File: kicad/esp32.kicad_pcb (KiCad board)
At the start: 2 copper layers, 85 x 75 mm, 75 parts, among them J1 5 / 12V, J10 Red, J11 Green, J12 Blue, J13 White, J14 Pad, J15 CONN FT232RL, J16 RJ12-I2C, J17 RJ12-I2C, J18 BATT, J2 +12V, J3 Onewire, J4 Onewire, J5 hole, J6 hole, J7 hole, J8 hole, J9 IO_RGBW, Q1 BSP75, Q2 BSP75, Q3 BSP75, Q4 BSP75, SW1 RESET, SW2 PROG, U1 ESP32-WROOM-32U, U2 MS5637, U3 Si7020-A20, U4 MCP73831-2, U5 ACT4088, U6 ACT4088

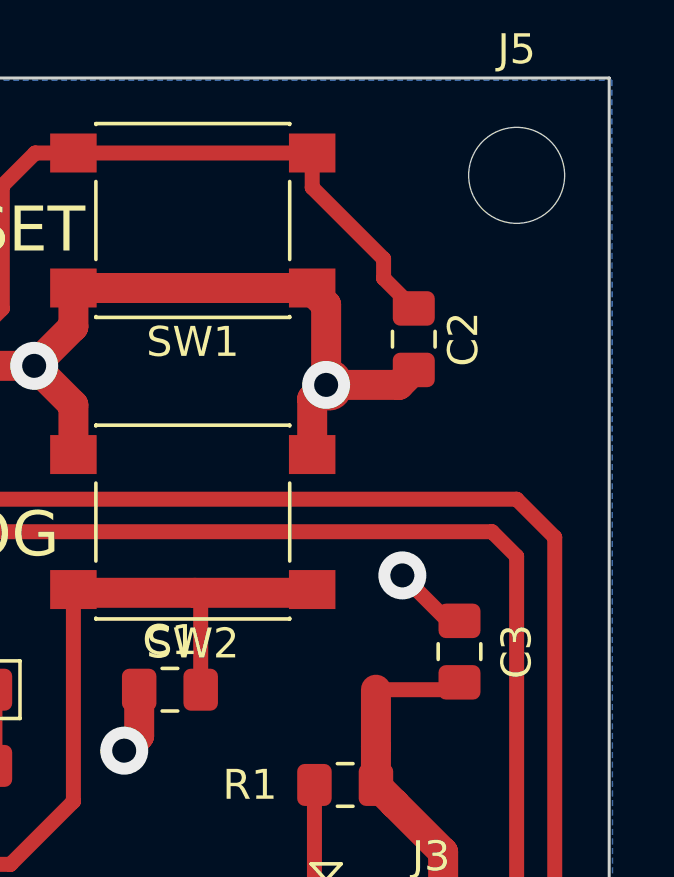
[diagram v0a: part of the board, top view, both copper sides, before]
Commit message: fix: pullup on reset close: https://github.com/Hackuarium/esp-32wroom/issues/1
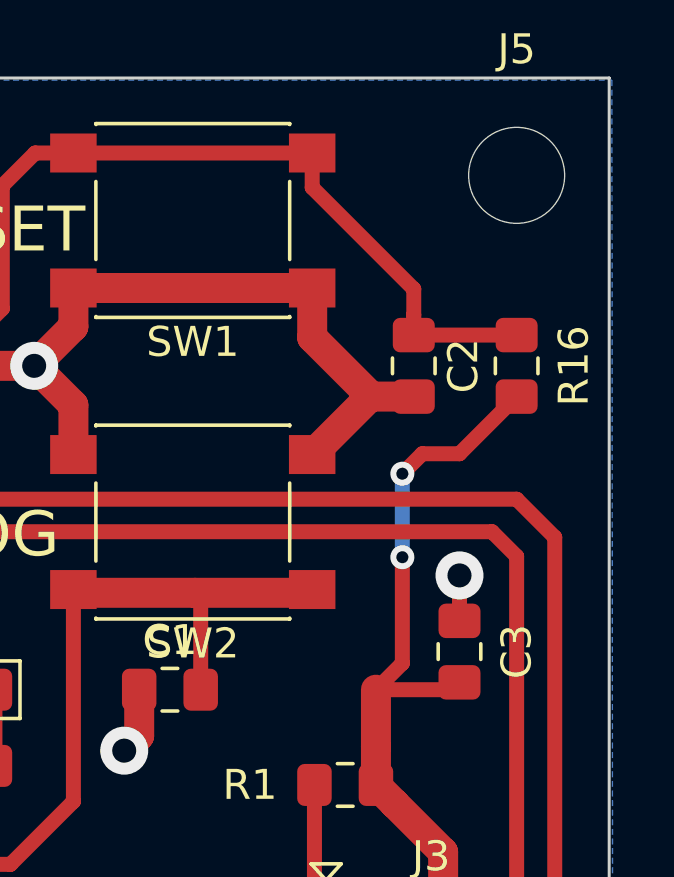
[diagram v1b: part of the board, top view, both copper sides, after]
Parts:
- added R16: 10k, Resistor_SMD:R_0805_2012Metric_Pad1.15x1.40mm_HandSolder, F.Cu at (159.9, 71.6)
- moved C2 0.89 mm to (156.5, 71.6)
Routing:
- net +3V3: track 158.4 -> 170.8 mm, vias 0 -> 2
- net /RST: track 46.0 -> 50.3 mm
- net GND: track 125.5 -> 123.7 mm, vias 23 -> 22
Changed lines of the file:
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@@
     (thickness 1.6)
     (drawings 56)
-    (tracks 621)
+    (tracks 625)
     (zones 0)
-    (modules 75)
+    (modules 76)
     (nets 73)
   )
@@
     (add_net "Net-(U6-Pad3)")
   )
+  (module Resistor_SMD:R_0805_2012Metric_Pad1.15x1.40mm_HandSolder (layer F.Cu)
+    (at 159.915 71.595 90)
+    (descr "Resistor SMD 0805 (2012 Metric), square (rectangular) end terminal, IPC_7351 nominal with elongated pad for handsoldering. (Body size source: https://docs.google.com/spreadsheets/d/1BsfQQcO9C6DZCsRaXUlFlo91Tg2WpOkGARC1WS5S8t0/edit?usp=sharing), generated with kicad-footprint-generator")
+    (tags "resistor handsolder")
+    (attr smd)
+    (fp_text reference R16 (at 0 1.905 90) (layer F.SilkS)
+      (effects (font (size 1 1) (thickness 0.15)))
+    )
+    (fp_text value 10k (at 0 1.65 90) (layer F.Fab)
+      (effects (font (size 1 1) (thickness 0.15)))
+    )
+    (fp_text user %R (at 0 0 90) (layer F.Fab)
+      (effects (font (size 0.5 0.5) (thickness 0.08)))
+    )
+    (fp_line (start 1.85 0.95) (end -1.85 0.95) (layer F.CrtYd) (width 0.05))
+    (fp_line (start 1.85 -0.95) (end 1.85 0.95) (layer F.CrtYd) (width 0.05))
+    (fp_line (start -1.85 -0.95) (end 1.85 -0.95) (layer F.CrtYd) (width 0.05))
+    (fp_line (start -1.85 0.95) (end -1.85 -0.95) (layer F.CrtYd) (width 0.05))
+    (fp_line (start -0.261252 0.71) (end 0.261252 0.71) (layer F.SilkS) (width 0.12))
+    (fp_line (start -0.261252 -0.71) (end 0.261252 -0.71) (layer F.SilkS) (width 0.12))
+    (fp_line (start 1 0.6) (end -1 0.6) (layer F.Fab) (width 0.1))
+    (fp_line (start 1 -0.6) (end 1 0.6) (layer F.Fab) (width 0.1))
+    (fp_line (start -1 -0.6) (end 1 -0.6) (layer F.Fab) (width 0.1))
+    (fp_line (start -1 0.6) (end -1 -0.6) (layer F.Fab) (width 0.1))
+    (pad 2 smd roundrect (at 1.025 0 90) (size 1.15 1.4) (layers F.Cu F.Paste F.Mask) (roundrect_rratio 0.217391)
+      (net 10 /RST))
+    (pad 1 smd roundrect (at -1.025 0 90) (size 1.15 1.4) (layers F.Cu F.Paste F.Mask) (roundrect_rratio 0.217391)
+      (net 3 +3V3))
+    (model ${KISYS3DMOD}/Resistor_SMD.3dshapes/R_0805_2012Metric.wrl
+      (at (xyz 0 0 0))
+      (scale (xyz 1 1 1))
+      (rotate (xyz 0 0 0))
+    )
+  )
   (module Diode_SMD:D_SOD-123 (layer F.Cu)
     (at 96.669 71.595 180)
@@
   )
   (module Capacitor_SMD:C_0805_2012Metric_Pad1.15x1.40mm_HandSolder (layer F.Cu)
-    (at 156.486 70.706 270)
+    (at 156.486 71.595 270)
     (descr "Capacitor SMD 0805 (2012 Metric), square (rectangular) end terminal, IPC_7351 nominal with elongated pad for handsoldering. (Body size source: https://docs.google.com/spreadsheets/d/1BsfQQcO9C6DZCsRaXUlFlo91Tg2WpOkGARC1WS5S8t0/edit?usp=sharing), generated with kicad-footprint-generator")
     (tags "capacitor handsolder")
@@
   (via (at 140.23 121.285) (size 2.4) (drill 1.2) (layers F.Cu B.Cu) (net 1))
   (segment (start 140.23 130.885) (end 140.23 123.665) (width 1.5) (layer F.Cu) (net 1))
-  (via (at 153.565 72.23) (size 1.6) (drill 0.8) (layers F.Cu B.Cu) (net 1))
-  (segment (start 153.67 72.335) (end 153.565 72.23) (width 1.5) (layer F.Cu) (net 1))
-  (segment (start 153.67 72.125) (end 153.565 72.23) (width 1.5) (layer F.Cu) (net 1))
   (segment (start 152.84 130.83) (end 153.385 130.83) (width 0.5) (layer F.Cu) (net 1))
   (segment (start 103.663 70.325) (end 104.06 70.325) (width 1) (layer F.Cu) (net 1))
@@
   (segment (start 102.638 76.929) (end 102.638 74.981) (width 0.5) (layer F.Cu) (net 1))
   (segment (start 101.622 77.945) (end 102.638 76.929) (width 0.5) (layer F.Cu) (net 1))
-  (via (at 156.105 78.58) (size 1.6) (drill 0.8) (layers F.Cu B.Cu) (net 1))
   (segment (start 158.01 80.095) (end 157.62 80.095) (width 0.5) (layer F.Cu) (net 1))
-  (segment (start 157.62 80.095) (end 156.105 78.58) (width 0.5) (layer F.Cu) (net 1))
   (via (at 147.391117 120.528884) (size 1.6) (drill 0.8) (layers F.Cu B.Cu) (net 1))
   (segment (start 146.31 121.395) (end 146.525001 121.395) (width 0.5) (layer F.Cu) (net 1))
@@
   (segment (start 140.23 121.285) (end 140.23 123.665) (width 1.5) (layer F.Cu) (net 1))
   (segment (start 145.14 69) (end 153.002 69) (width 1) (layer F.Cu) (net 1))
-  (segment (start 153.002 69) (end 153.565 69.563) (width 1) (layer F.Cu) (net 1))
-  (segment (start 153.81 72.475) (end 153.565 72.23) (width 0.5) (layer F.Cu) (net 1))
   (segment (start 153.235 74.525) (end 153.1 74.66) (width 0.5) (layer F.Cu) (net 1))
-  (segment (start 153.1 72.695) (end 153.565 72.23) (width 1) (layer F.Cu) (net 1))
-  (segment (start 153.1 74.552) (end 153.1 72.695) (width 1) (layer F.Cu) (net 1))
   (segment (start 145.14 72.902) (end 145.14 74.552) (width 1) (layer F.Cu) (net 1))
   (segment (start 143.833 71.595) (end 145.14 72.902) (width 1) (layer F.Cu) (net 1))
@@
   (segment (start 123.085 87.597) (end 123.974 86.708) (width 0.5) (layer F.Cu) (net 1))
   (segment (start 123.085 89.105) (end 123.085 87.597) (width 0.5) (layer F.Cu) (net 1))
-  (segment (start 153.565 69.563) (end 153.565 72.23) (width 1) (layer F.Cu) (net 1))
-  (segment (start 155.987 72.23) (end 156.486 71.731) (width 1) (layer F.Cu) (net 1))
-  (segment (start 153.565 72.23) (end 155.987 72.23) (width 1) (layer F.Cu) (net 1))
   (segment (start 92.605 73.355) (end 92.115 72.865) (width 1) (layer F.Cu) (net 1))
   (segment (start 92.605 75.65) (end 92.605 73.355) (width 1) (layer F.Cu) (net 1))
@@
   (segment (start 114.359999 86.670001) (end 113.724999 86.670001) (width 1) (layer F.Cu) (net 1))
   (segment (start 115.220001 86.670001) (end 114.359999 86.670001) (width 1) (layer F.Cu) (net 1))
+  (segment (start 155.032 72.62) (end 153.1 74.552) (width 1) (layer F.Cu) (net 1))
+  (segment (start 156.486 72.62) (end 155.032 72.62) (width 1) (layer F.Cu) (net 1))
+  (segment (start 155.032 72.582) (end 155.032 72.62) (width 1) (layer F.Cu) (net 1))
+  (segment (start 153.1 70.65) (end 155.032 72.582) (width 1) (layer F.Cu) (net 1))
+  (segment (start 153.1 69) (end 153.1 70.65) (width 1) (layer F.Cu) (net 1))
+  (via (at 158.01 78.58) (size 1.6) (drill 0.8) (layers F.Cu B.Cu) (net 1))
+  (segment (start 158.01 80.095) (end 158.01 78.58) (width 0.5) (layer F.Cu) (net 1))
   (segment (start 103.738 72.931) (end 103.588 72.781) (width 1) (layer F.Cu) (net 2))
   (segment (start 107.1 72.931) (end 103.738 72.931) (width 1) (layer F.Cu) (net 2))
@@
   (segment (start 116.06 83.7) (end 116.49 84.13) (width 1) (layer F.Cu) (net 3))
   (segment (start 115.385 83.025) (end 116.06 83.7) (width 1) (layer F.Cu) (net 3))
+  (segment (start 159.915 72.62) (end 158.01 74.525) (width 0.5) (layer F.Cu) (net 3))
+  (via (at 156.105 75.19) (size 0.8) (drill 0.4) (layers F.Cu B.Cu) (net 3))
+  (segment (start 156.77 74.525) (end 156.105 75.19) (width 0.5) (layer F.Cu) (net 3))
+  (segment (start 158.01 74.525) (end 156.77 74.525) (width 0.5) (layer F.Cu) (net 3))
+  (via (at 156.105 77.974) (size 0.8) (drill 0.4) (layers F.Cu B.Cu) (net 3))
+  (segment (start 156.105 75.19) (end 156.105 77.974) (width 0.5) (layer B.Cu) (net 3))
+  (segment (start 156.105 81.51) (end 155.225 82.39) (width 0.5) (layer F.Cu) (net 3))
+  (segment (start 156.105 77.974) (end 156.105 81.51) (width 0.5) (layer F.Cu) (net 3))
   (segment (start 96.209919 62.578) (end 95.145 63.642919) (width 0.5) (layer B.Cu) (net 4))
   (segment (start 130.578 73.754) (end 130.578 71.722) (width 0.5) (layer B.Cu) (net 4))
@@
   (segment (start 145.14 64.5) (end 143.865 64.5) (width 0.5) (layer F.Cu) (net 10))
   (segment (start 145.14 64.5) (end 153.074 64.5) (width 0.5) (layer F.Cu) (net 10))
-  (segment (start 153.1 65.65) (end 155.48 68.03) (width 0.5) (layer F.Cu) (net 10))
-  (segment (start 153.1 64.5) (end 153.1 65.65) (width 0.5) (layer F.Cu) (net 10))
   (segment (start 141.85999 70.60001) (end 142.77 69.69) (width 0.5) (layer F.Cu) (net 10))
   (segment (start 142.77 65.595) (end 142.77 69.69) (width 0.5) (layer F.Cu) (net 10))
@@
   (segment (start 132.499998 74.135) (end 136.034988 70.60001) (width 0.5) (layer F.Cu) (net 10))
   (segment (start 120.3 74.135) (end 132.499998 74.135) (width 0.5) (layer F.Cu) (net 10))
-  (segment (start 155.48 68.675) (end 155.48 68.03) (width 0.5) (layer F.Cu) (net 10))
-  (segment (start 156.486 69.681) (end 155.48 68.675) (width 0.5) (layer F.Cu) (net 10))
+  (segment (start 156.486 69.036) (end 156.486 69.895) (width 0.5) (layer F.Cu) (net 10))
+  (segment (start 153.1 65.65) (end 156.486 69.036) (width 0.5) (layer F.Cu) (net 10))
+  (segment (start 156.486 69.895) (end 156.486 70.57) (width 0.5) (layer F.Cu) (net 10))
+  (segment (start 153.1 64.5) (end 153.1 65.65) (width 0.5) (layer F.Cu) (net 10))
+  (segment (start 156.486 70.57) (end 159.915 70.57) (width 0.5) (layer F.Cu) (net 10))
   (via (at 144.672207 134.457207) (size 1.6) (drill 0.8) (layers F.Cu B.Cu) (net 11))
   (segment (start 144.675 134.46) (end 144.672207 134.457207) (width 0.5) (layer F.Cu) (net 11))

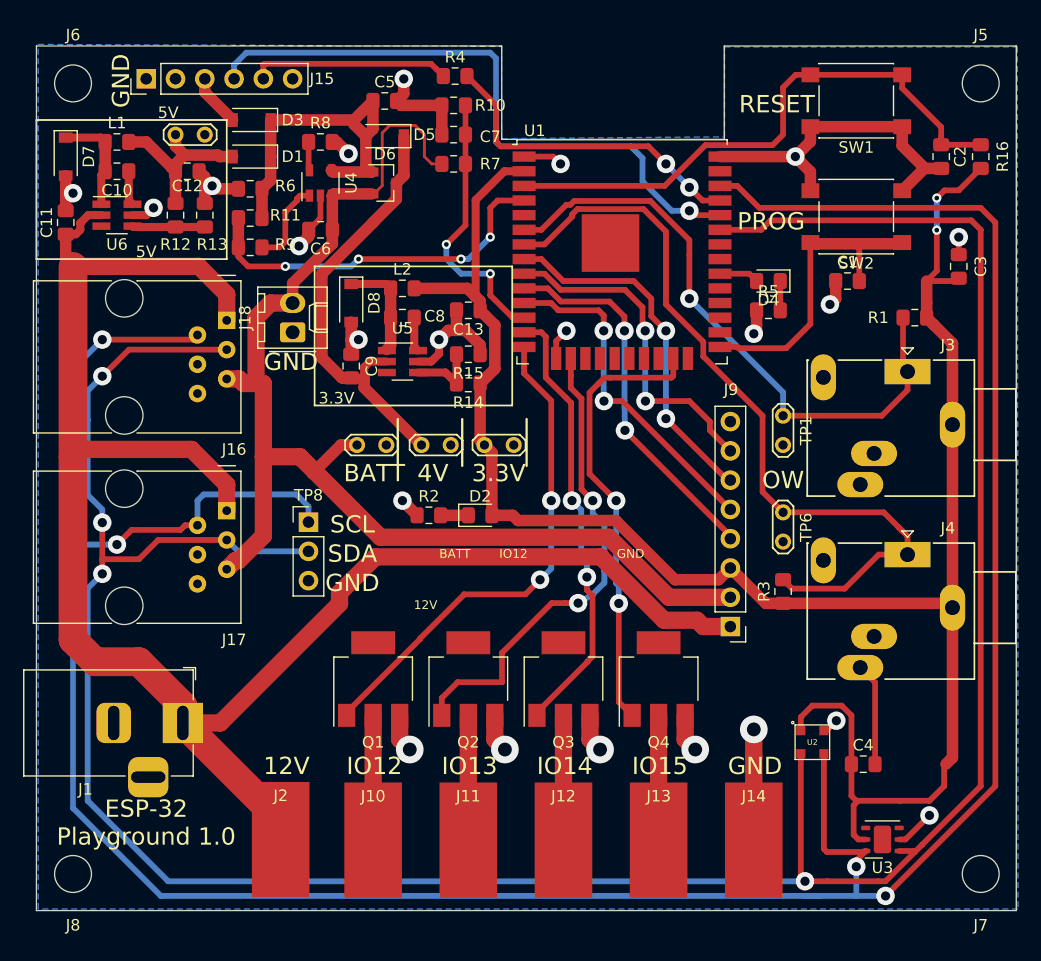
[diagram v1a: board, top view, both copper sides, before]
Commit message: feat: add light and temperature sensors. closes https://github.com/Hackuarium/esp-32wroom/issues/6 and https://github.com/Hackuarium/esp-32wroom/issues/5
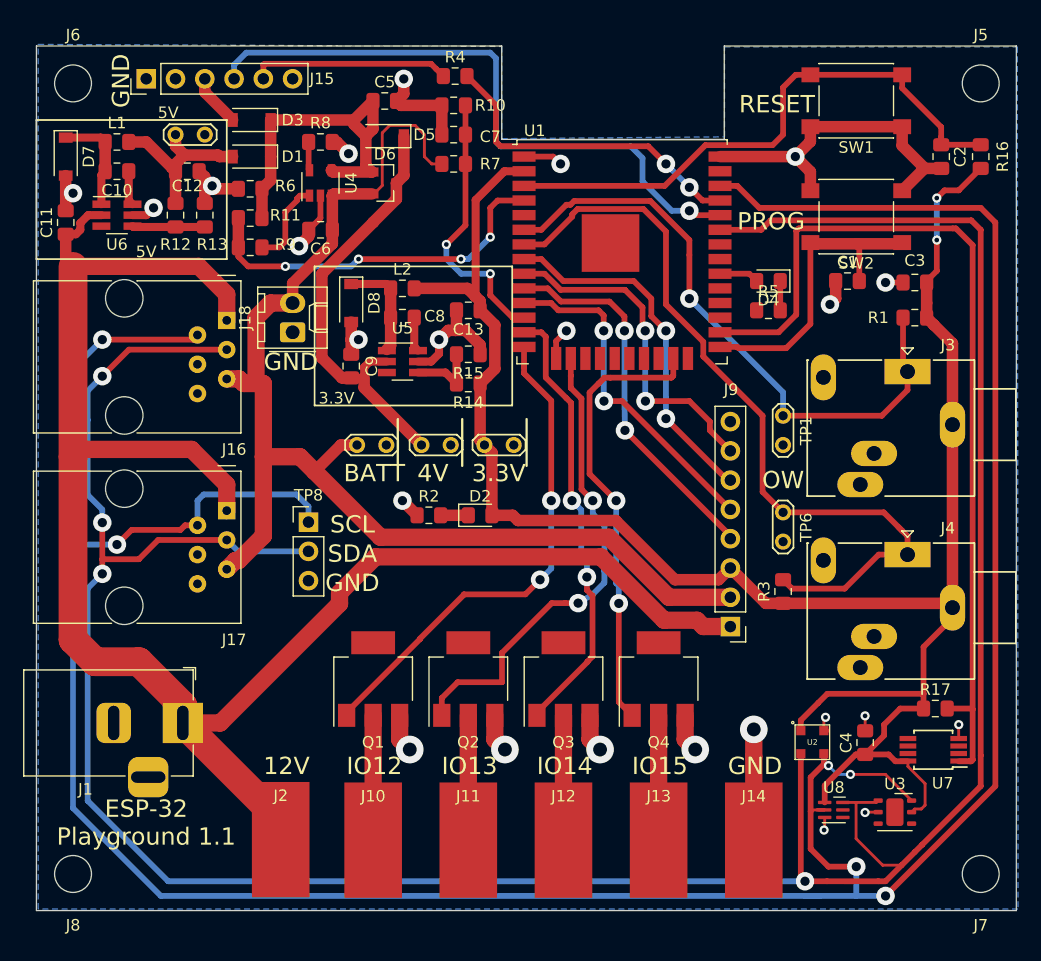
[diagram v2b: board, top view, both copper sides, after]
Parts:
- added R17: 4.7k, Resistor_SMD:R_0805_2012Metric_Pad1.15x1.40mm_HandSolder, F.Cu at (156.0, 119.5)
- added U7: DS18B20U, Package_SO:MSOP-8_3x3mm_P0.65mm, F.Cu at (155.8, 123.0)
- added U8: TCS3400, OptoDevice:Broadcom_DFN-6_2x2mm_P0.65mm, F.Cu at (147.2, 128.3)
- moved C3 4.06 mm to (154.2, 82.5), turned to 180 degrees
- moved U3 2.60 mm to (152.5, 128.5), turned to 0 degrees
- moved C4 1.88 mm to (149.9, 122.4), turned to 90 degrees
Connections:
- net /SCL renamed SCL
- net /SDA renamed SDA
- U1 pad 26: Net-(U1-Pad26) -> ONE3
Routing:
- net ONE3: track 0.00 -> 79.0 mm
- net SCL: track 254.1 -> 265.1 mm, vias 4 -> 6
- net SDA: track 237.1 -> 246.9 mm
- net GND: track 123.7 -> 113.9 mm, vias 22 -> 24
- net +3V3: track 170.8 -> 171.6 mm
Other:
- board text added: "ESP-32 Playground 1.1"
- board text removed: "ESP-32 Playground 1.0"
